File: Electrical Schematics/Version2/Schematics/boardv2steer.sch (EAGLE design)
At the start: 20 parts, among them IC3 VNH2SP30-E, J2 PHOENIX_2POS_1792863, Q1 IRFR3707Z, Q2 IRFR3707Z, U1 ADS1225_RGV_16

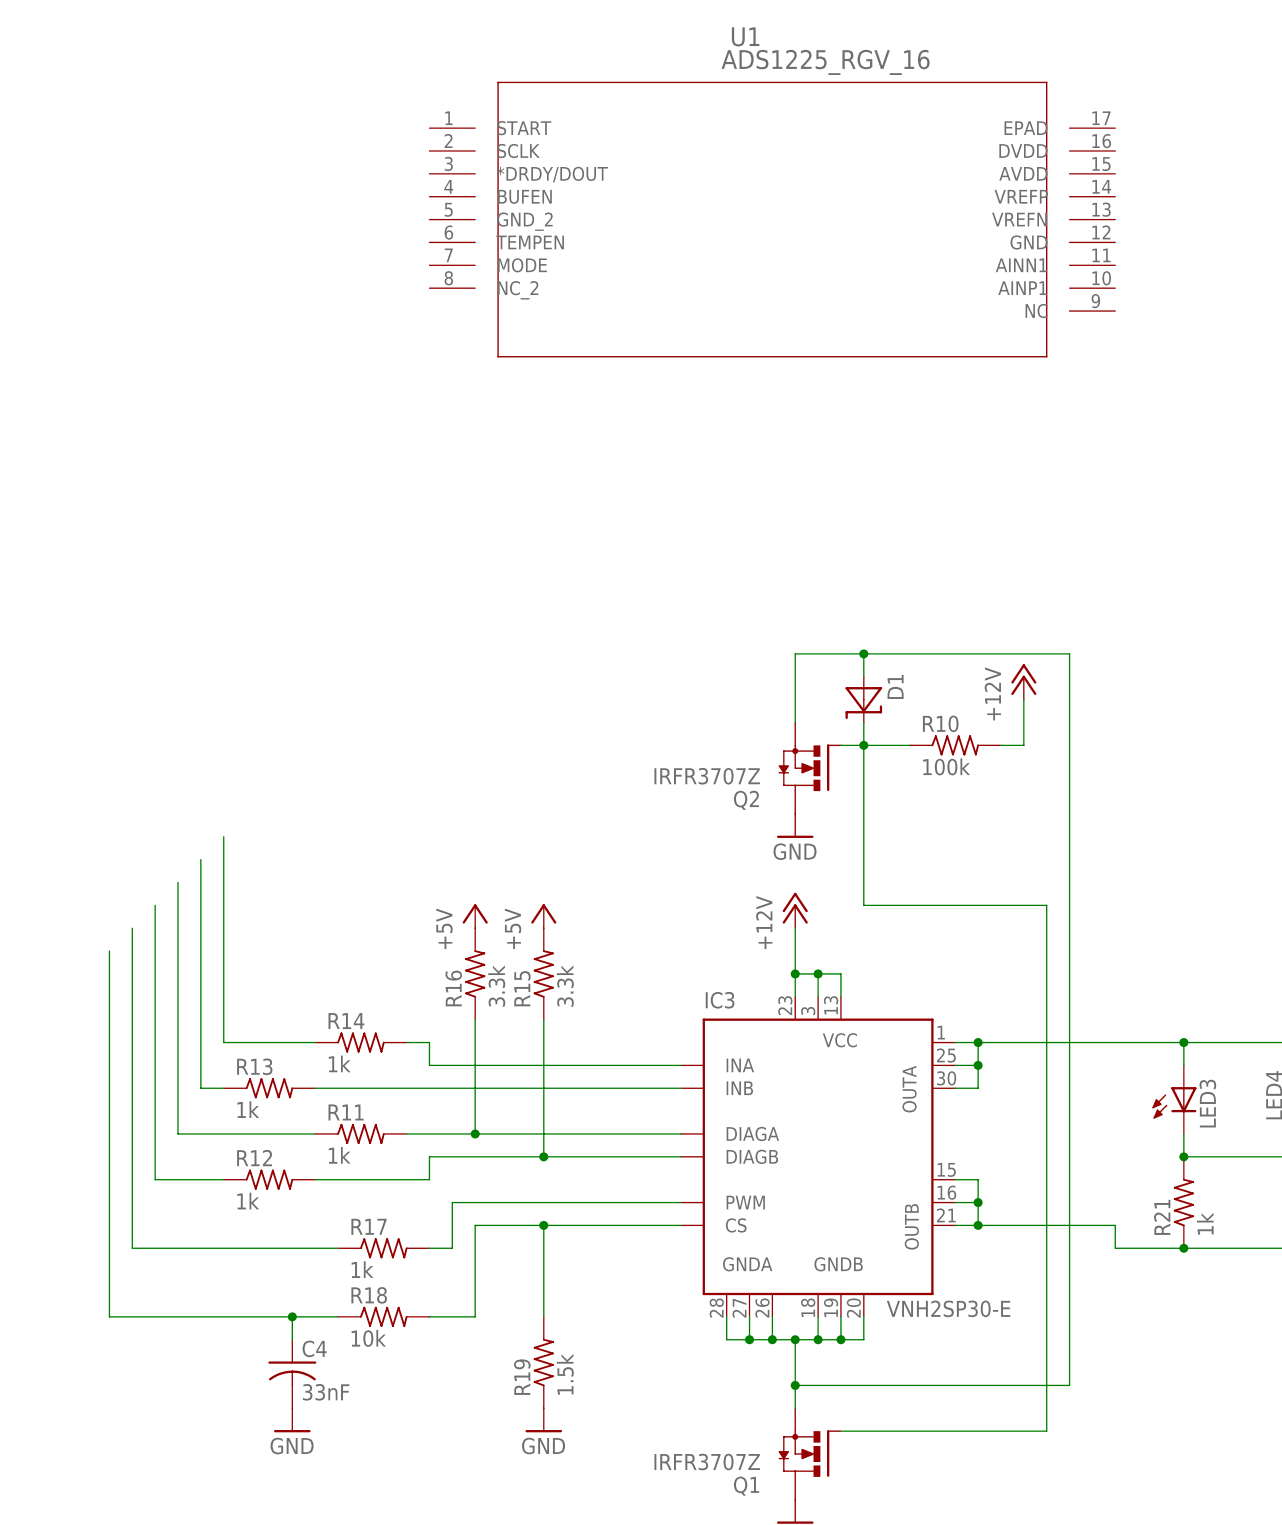
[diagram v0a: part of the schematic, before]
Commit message: updated the schematics for the ridgley
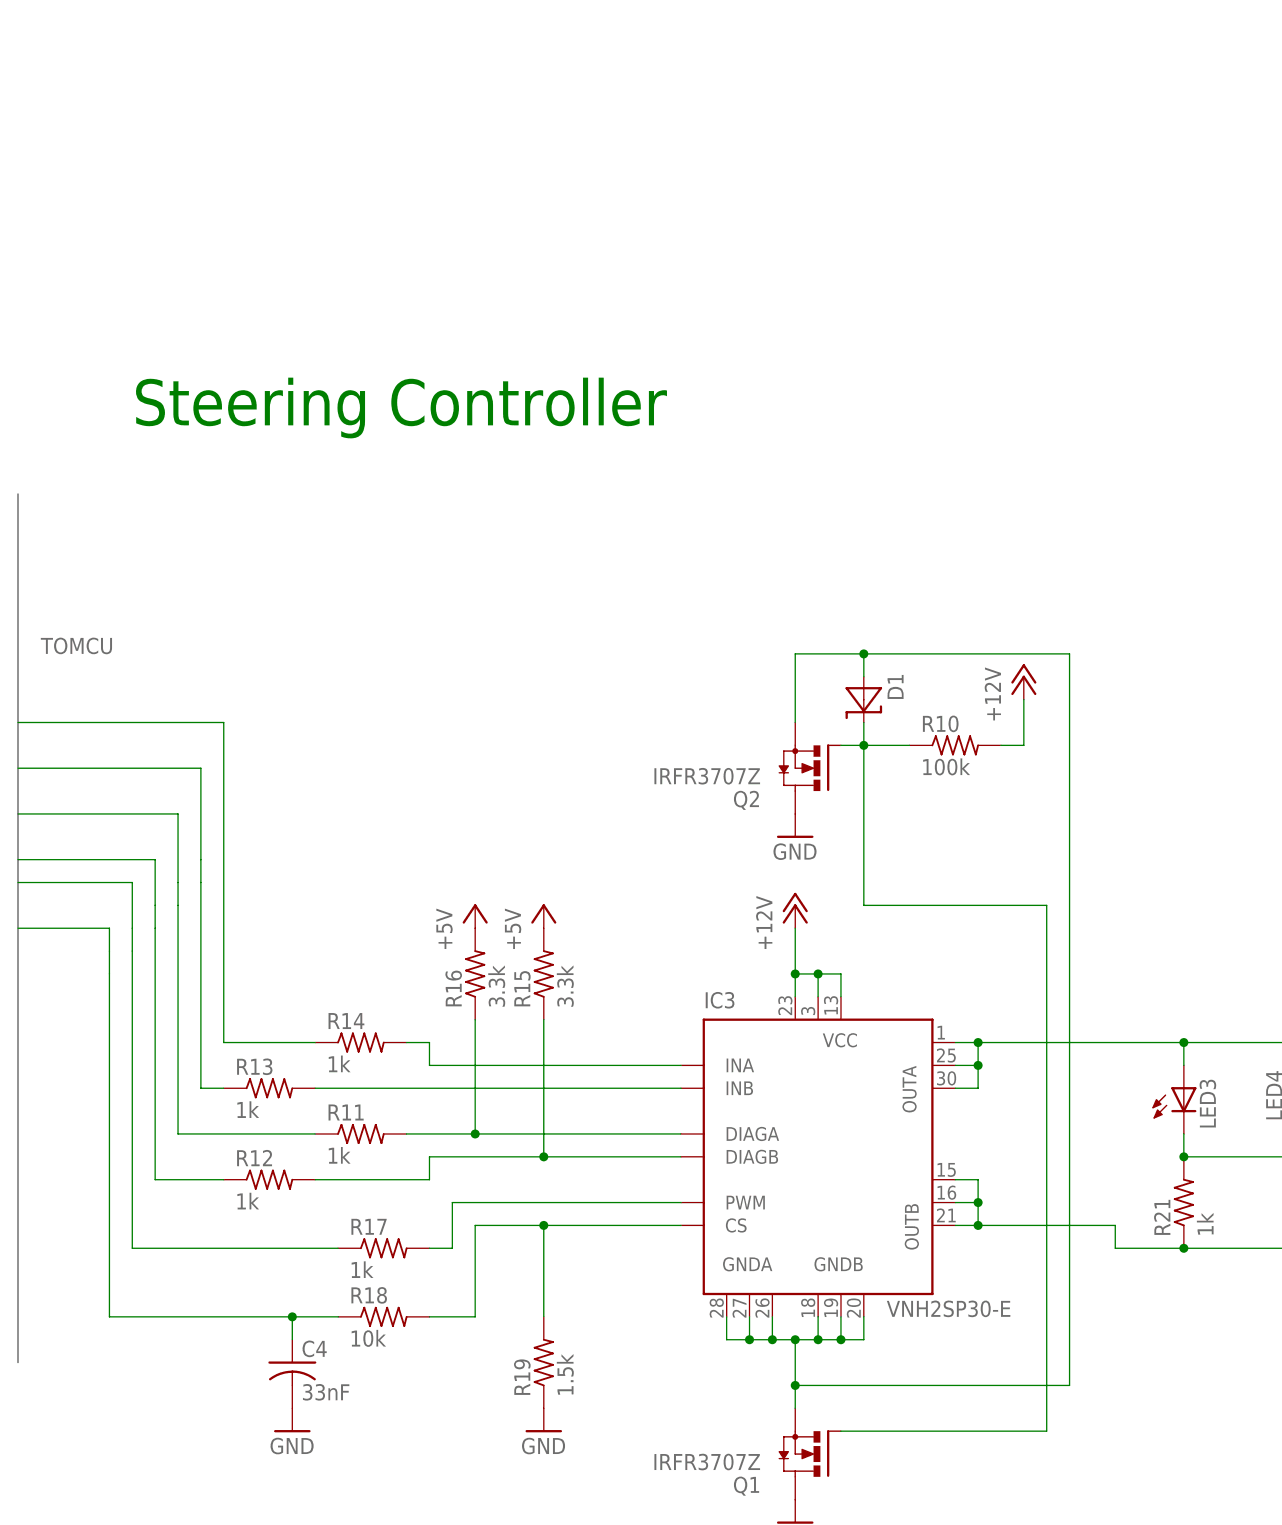
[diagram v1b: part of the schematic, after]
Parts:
- removed U1: ADS1225_RGV_16, shit:ADS1225_RGV_16
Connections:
- removed net N$12: R14.1
- removed net N$23: C4.1, R18.1
- removed net N$29: R13.1
- removed net N$30: R11.1
- removed net N$31: R12.1
- removed net N$32: R17.1
- new net B$1: C4.1, R11.1, R12.1, R13.1, R14.1, R17.1, R18.1
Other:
- note added: "Steering Controller"
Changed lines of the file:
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@@
 <part name="R21" library="rcl" deviceset="R-US_" device="R1206W" value="1k"/>
 <part name="J2" library="Atlanta-Robotics LAPTOP" deviceset="PHOENIX_2POS_1792863" device="" value=""/>
-<part name="U1" library="shit" deviceset="ADS1225_RGV_16" device=""/>
+<part name="FRAME1" library="frames" deviceset="DOCFIELD" device=""/>
 </parts>
 <sheets>
 <sheet>
 <plain>
+<text x="-76.2" y="114.3" size="5.08" layer="91">Steering Controller</text>
+<frame x1="-101.6" y1="-58.42" x2="190.5" y2="127" columns="8" rows="5" layer="91"/>
 </plain>
 <instances>
@@
 <instance part="J2" gate="G$1" x="60.96" y="45.72" rot="R180"/>
 <instance part="J2" gate="G$2" x="60.96" y="22.86" rot="R180"/>
-<instance part="U1" gate="A" x="-43.18" y="147.32"/>
+<instance part="FRAME1" gate="G$1" x="83.82" y="-53.34"/>
 </instances>
 <busses>
+<bus name="TOMCU">
+<segment>
+<wire x1="-88.9" y1="106.68" x2="-88.9" y2="10.16" width="0.762" layer="92"/>
+<label x="-86.36" y="88.9" size="1.778" layer="95"/>
+</segment>
+</bus>
 </busses>
 <nets>
@@
 </segment>
 </net>
-<net name="N$23" class="0">
-<segment>
-<pinref part="R18" gate="G$1" pin="1"/>
-<wire x1="-53.34" y1="15.24" x2="-58.42" y2="15.24" width="0.1524" layer="91"/>
-<pinref part="C4" gate="G$1" pin="1"/>
-<wire x1="-58.42" y1="15.24" x2="-78.74" y2="15.24" width="0.1524" layer="91"/>
-<wire x1="-58.42" y1="12.7" x2="-58.42" y2="15.24" width="0.1524" layer="91"/>
-<junction x="-58.42" y="15.24"/>
-<wire x1="-78.74" y1="15.24" x2="-78.74" y2="55.88" width="0.1524" layer="91"/>
-</segment>
-</net>
 <net name="N$24" class="0">
 <segment>
@@
 </segment>
 </net>
-<net name="N$29" class="0">
-<segment>
-<pinref part="R13" gate="G$1" pin="1"/>
-<wire x1="-66.04" y1="40.64" x2="-68.58" y2="40.64" width="0.1524" layer="91"/>
-<wire x1="-68.58" y1="40.64" x2="-68.58" y2="66.04" width="0.1524" layer="91"/>
-</segment>
-</net>
-<net name="N$30" class="0">
-<segment>
-<pinref part="R11" gate="G$1" pin="1"/>
-<wire x1="-55.88" y1="35.56" x2="-71.12" y2="35.56" width="0.1524" layer="91"/>
-<wire x1="-71.12" y1="35.56" x2="-71.12" y2="63.5" width="0.1524" layer="91"/>
-</segment>
-</net>
-<net name="N$31" class="0">
-<segment>
-<pinref part="R12" gate="G$1" pin="1"/>
-<wire x1="-66.04" y1="30.48" x2="-73.66" y2="30.48" width="0.1524" layer="91"/>
-<wire x1="-73.66" y1="30.48" x2="-73.66" y2="60.96" width="0.1524" layer="91"/>
-</segment>
-</net>
-<net name="N$32" class="0">
-<segment>
-<pinref part="R17" gate="G$1" pin="1"/>
-<wire x1="-53.34" y1="22.86" x2="-76.2" y2="22.86" width="0.1524" layer="91"/>
-<wire x1="-76.2" y1="22.86" x2="-76.2" y2="58.42" width="0.1524" layer="91"/>
-</segment>
-</net>
 <net name="N$28" class="0">
 <segment>
@@
 </segment>
 </net>
-<net name="N$12" class="0">
+<net name="B$1" class="0">
+<segment>
+<pinref part="R18" gate="G$1" pin="1"/>
+<wire x1="-53.34" y1="15.24" x2="-58.42" y2="15.24" width="0.1524" layer="91"/>
+<pinref part="C4" gate="G$1" pin="1"/>
+<wire x1="-58.42" y1="15.24" x2="-78.74" y2="15.24" width="0.1524" layer="91"/>
+<wire x1="-58.42" y1="12.7" x2="-58.42" y2="15.24" width="0.1524" layer="91"/>
+<junction x="-58.42" y="15.24"/>
+<wire x1="-78.74" y1="15.24" x2="-78.74" y2="53.34" width="0.1524" layer="91"/>
+<wire x1="-78.74" y1="53.34" x2="-78.74" y2="55.88" width="0.1524" layer="91"/>
+<wire x1="-88.9" y1="58.42" x2="-78.74" y2="58.42" width="0.1524" layer="91"/>
+<wire x1="-78.74" y1="58.42" x2="-78.74" y2="55.88" width="0.1524" layer="91"/>
+</segment>
+<segment>
+<pinref part="R17" gate="G$1" pin="1"/>
+<wire x1="-53.34" y1="22.86" x2="-76.2" y2="22.86" width="0.1524" layer="91"/>
+<wire x1="-76.2" y1="22.86" x2="-76.2" y2="55.88" width="0.1524" layer="91"/>
+<wire x1="-76.2" y1="55.88" x2="-76.2" y2="58.42" width="0.1524" layer="91"/>
+<wire x1="-88.9" y1="63.5" x2="-76.2" y2="63.5" width="0.1524" layer="91"/>
+<wire x1="-76.2" y1="63.5" x2="-76.2" y2="58.42" width="0.1524" layer="91"/>
+</segment>
+<segment>
+<pinref part="R12" gate="G$1" pin="1"/>
+<wire x1="-66.04" y1="30.48" x2="-73.66" y2="30.48" width="0.1524" layer="91"/>
+<wire x1="-73.66" y1="30.48" x2="-73.66" y2="58.42" width="0.1524" layer="91"/>
+<wire x1="-73.66" y1="58.42" x2="-73.66" y2="60.96" width="0.1524" layer="91"/>
+<wire x1="-88.9" y1="66.04" x2="-73.66" y2="66.04" width="0.1524" layer="91"/>
+<wire x1="-73.66" y1="66.04" x2="-73.66" y2="60.96" width="0.1524" layer="91"/>
+</segment>
+<segment>
+<pinref part="R11" gate="G$1" pin="1"/>
+<wire x1="-55.88" y1="35.56" x2="-71.12" y2="35.56" width="0.1524" layer="91"/>
+<wire x1="-71.12" y1="35.56" x2="-71.12" y2="60.96" width="0.1524" layer="91"/>
+<wire x1="-71.12" y1="60.96" x2="-71.12" y2="63.5" width="0.1524" layer="91"/>
+<wire x1="-88.9" y1="71.12" x2="-71.12" y2="71.12" width="0.1524" layer="91"/>
+<wire x1="-71.12" y1="71.12" x2="-71.12" y2="63.5" width="0.1524" layer="91"/>
+</segment>
+<segment>
+<pinref part="R13" gate="G$1" pin="1"/>
+<wire x1="-66.04" y1="40.64" x2="-68.58" y2="40.64" width="0.1524" layer="91"/>
+<wire x1="-68.58" y1="40.64" x2="-68.58" y2="63.5" width="0.1524" layer="91"/>
+<wire x1="-68.58" y1="63.5" x2="-68.58" y2="66.04" width="0.1524" layer="91"/>
+<wire x1="-88.9" y1="76.2" x2="-68.58" y2="76.2" width="0.1524" layer="91"/>
+<wire x1="-68.58" y1="76.2" x2="-68.58" y2="66.04" width="0.1524" layer="91"/>
+</segment>
 <segment>
 <pinref part="R14" gate="G$1" pin="1"/>
 <wire x1="-55.88" y1="45.72" x2="-66.04" y2="45.72" width="0.1524" layer="91"/>
-<wire x1="-66.04" y1="45.72" x2="-66.04" y2="68.58" width="0.1524" layer="91"/>
-</segment>
-</net>
+<wire x1="-66.04" y1="45.72" x2="-66.04" y2="81.28" width="0.1524" layer="91"/>
+<wire x1="-88.9" y1="81.28" x2="-66.04" y2="81.28" width="0.1524" layer="91"/>
+</segment>
+</net>
